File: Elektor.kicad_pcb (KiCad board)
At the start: 2 copper layers, 50 x 42 mm, 63 parts, among them J1 Conn_Coaxial, Q1 BF545B, U1 Si5351A-B-GT, U2 74HC04, U3 74HC4066D_653, U5 MCP6022, U6 AUDIOSHIELD-REVD, U7 MCP6022, Y1 ABM7-25.000MHZ-D2Y-T

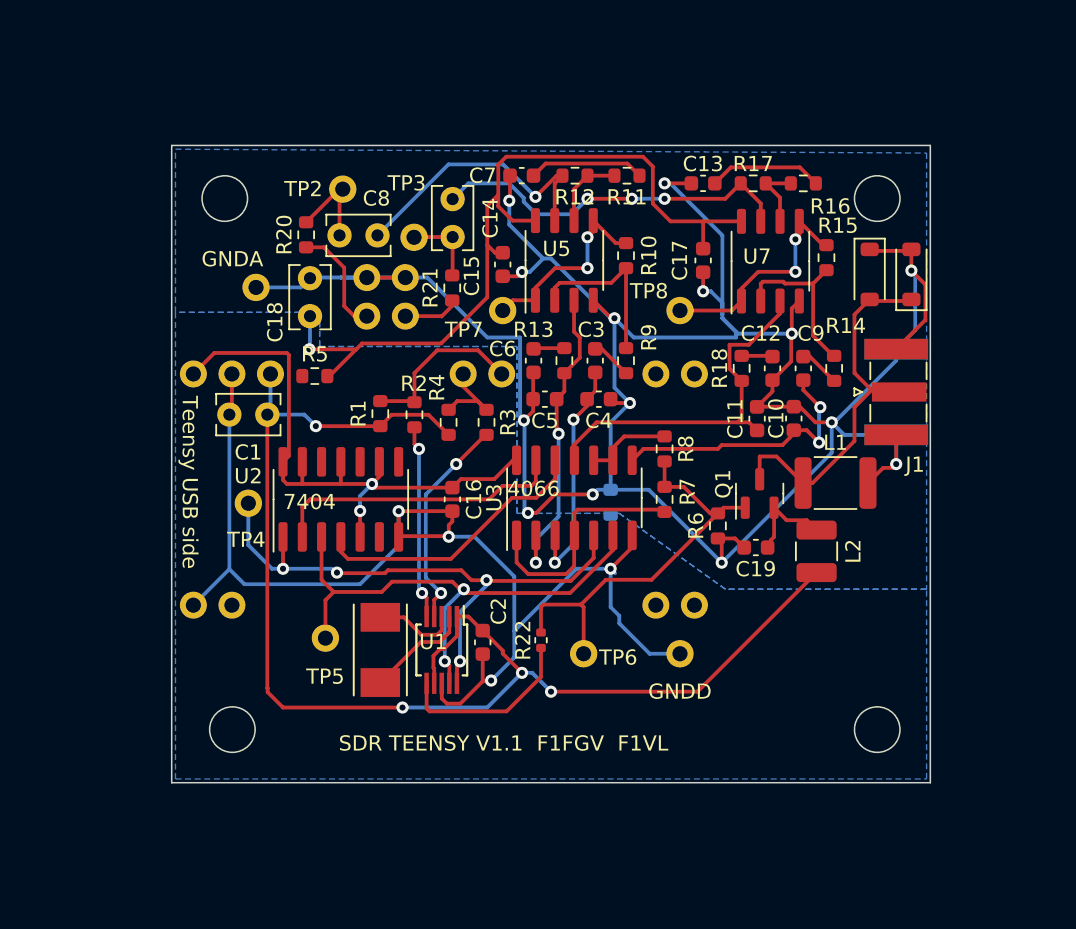
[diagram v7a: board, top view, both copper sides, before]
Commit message: version 2.0 using a SN74CBTLV3253
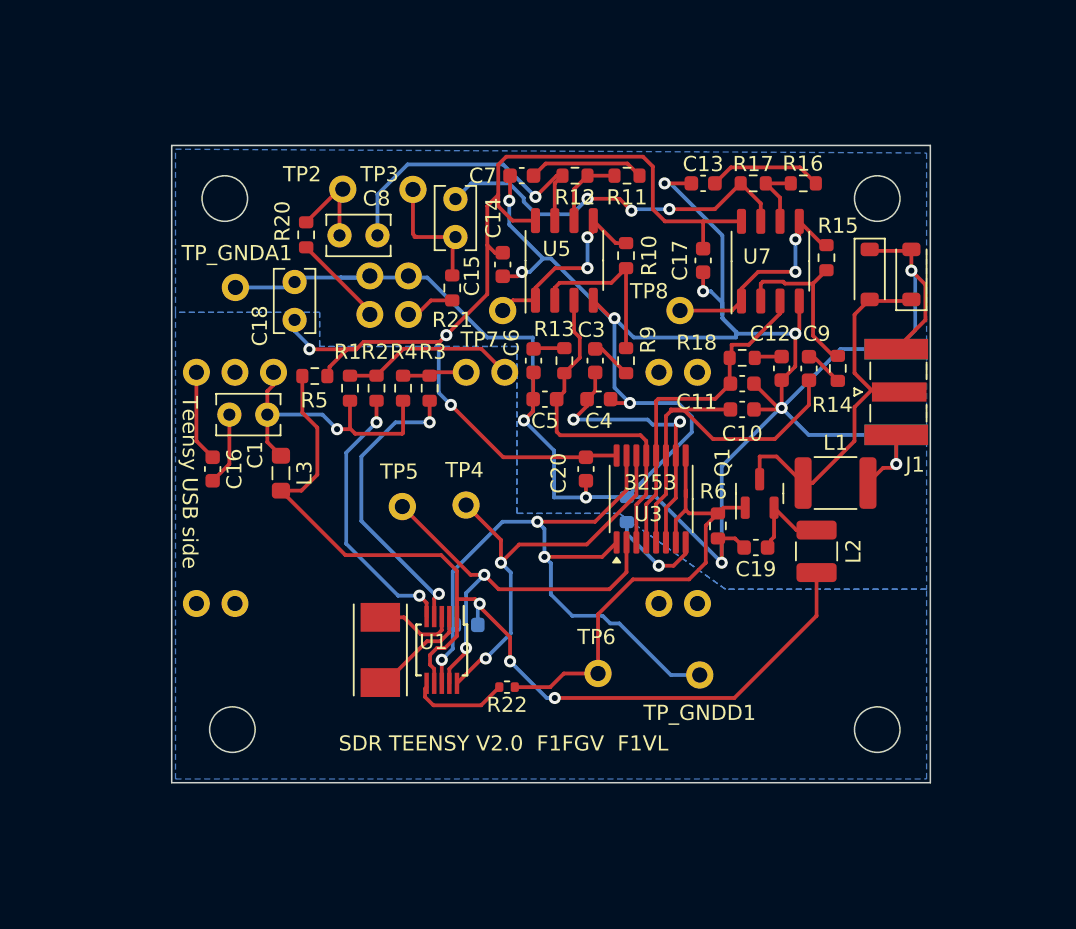
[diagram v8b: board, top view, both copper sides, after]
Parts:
- removed R7, R8: 100, Resistor_SMD:R_0603_1608Metric
- removed U2: 74HC04, Package_SO:SOIC-14_3.9x8.7mm_P1.27mm
- added C20: 100n, Capacitor_SMD:C_0603_1608Metric, F.Cu at (184.3, 82.3)
- added L3: 1uH, Inductor_SMD:L_0805_2012Metric_Pad1.05x1.20mm_HandSolder, F.Cu at (164.2, 82.6)
- C2: moved to B.Cu
- U3: value 74HC4066D_653 -> SN74CBTLV3253PW; footprint Package_SO:SOIC-14_3.9x8.7mm_P1.27mm -> Package_SO:TSSOP-16_4.4x5mm_P0.65mm
- moved C16 15.9 mm to (159.7, 82.3)
- moved TP4 14.3 mm to (176.4, 84.7)
- moved TP5 10.0 mm to (172.2, 84.8)
- moved U3 5.06 mm to (188.6, 84.3)
- moved R3 4.37 mm to (174.0, 77.0)
- moved R22 3.82 mm to (179.1, 96.7), turned to 180 degrees
- moved R2 3.75 mm to (172.2, 77.0)
- moved C10 3.45 mm to (194.6, 78.4), turned to 180 degrees
- moved TP3 3.16 mm to (172.9, 63.9)
- moved R4 3.05 mm to (170.5, 77.0)
- moved R1 2.61 mm to (168.8, 77.0)
- moved C11 2.51 mm to (194.6, 76.7), turned to 0 degrees
- moved TP_GNDD1 1.91 mm to (191.8, 95.9)
- moved TP6 1.61 mm to (185.1, 95.8)
- moved C2 1.59 mm to (176.4, 92.6), turned to 180 degrees
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- renumbered GNDA to TP_GNDA1, GNDD to TP_GNDD1
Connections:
- C1 pad 1: 3.3V -> Net-(C1-Pad1)
- C10 pad 2: Net-(U3-3Y) -> Net-(U3-1B2)
- C11 pad 1: Net-(U3-4Y) -> Net-(U3-1B3)
- C16 pad 1: Net-(U2G-VCC) -> Net-(C16-Pad1)
- C3 pad 1: Net-(U3-2Z) -> Net-(U3-1B1)
- C4 pad 2: Net-(U3-2Z) -> Net-(U3-1B1)
- C5 pad 1: Net-(U3-1Z) -> Net-(U3-1B4)
- C9 pad 1: Net-(U3-3Y) -> Net-(U3-1B2)
- R1 pad 1: 3.3V -> Net-(C1-Pad1)
- R13 pad 1: Net-(U3-1Z) -> Net-(U3-1B4)
- R18 pad 1: Net-(U3-4Y) -> Net-(U3-1B3)
- R19 pad 1: unconnected-(R19-Pad1) -> GND
- R2 pad 1: 3.3V -> Net-(C1-Pad1)
- R22 pad 1: Net-(U1-CLK2) -> Net-(Q1-S)
- R22 pad 2: Net-(Q1-S) -> Net-(U1-CLK2)
- U3 pad 1: Net-(U3-1Y) -> GND
- U3 pad 10: Net-(U3-3Z) -> Net-(U3-1B1)
- U3 pad 11: Net-(U3-4Y) -> Net-(U3-1B2)
- U3 pad 12: Net-(U3-4E) -> Net-(U3-1B3)
- U3 pad 13: Net-(U3-1E) -> Net-(U3-1B4)
- U3 pad 14: Net-(U2G-VCC) -> Net-(TP4-Pin_1)
- U3 pad 2: Net-(U3-1Z) -> Net-(TP5-Pin_1)
- U3 pad 3: Net-(U3-2Z) -> Net-(U3-1B4)
- U3 pad 4: Net-(U3-1Y) -> Net-(U3-1B3)
- U3 pad 5: Net-(TP4-Pin_1) -> Net-(U3-1B2)
- U3 pad 6: Net-(TP5-Pin_1) -> Net-(U3-1B1)
- U3 pad 7: GND -> Net-(Q1-S)
- U3 pad 8: Net-(U3-3Y) -> GND
- U3 pad 9: Net-(U3-3Z) -> Net-(Q1-S)
- U5 pad 3: Net-(U3-1Z) -> Net-(U3-1B4)
- U6 pad 3V: 3.3V -> Net-(C1-Pad1)
- U6 pad 5V: Net-(U2G-VCC) -> Net-(C16-Pad1)
- U7 pad 3: Net-(U3-4Y) -> Net-(U3-1B3)
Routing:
- net Net-(U2G-VCC): track 40.1 -> 0.00 mm, vias 2 -> 0
- net Net-(U3-1B2): track 0.00 -> 25.5 mm
- net Net-(U3-4Y): track 23.5 -> 0.00 mm
- net Net-(U3-1B4): track 0.00 -> 22.6 mm
- net GND: track 79.9 -> 57.4 mm
- net Net-(U3-1B3): track 0.00 -> 22.2 mm
- net Net-(U3-1Z): track 20.6 -> 0.00 mm, vias 2 -> 0
- net Net-(C1-Pad1): track 0.00 -> 19.5 mm, vias 0 -> 1
- net Net-(U3-1E): track 19.5 -> 0.00 mm
- net Net-(U3-1B1): track 0.00 -> 19.3 mm, vias 0 -> 2
- net 3.3V: track 86.3 -> 67.3 mm, vias 4 -> 3
- net Net-(U3-4E): track 18.7 -> 0.00 mm
- net Net-(U3-3Y): track 18.0 -> 0.00 mm, vias 2 -> 0
- net 3.3VA: track 52.9 -> 70.9 mm, vias 1 -> 3
- net Net-(U3-1Y): track 15.5 -> 0.00 mm
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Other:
- board text added: "3253"
- board text added: "SDR TEENSY V2.0 F1FGV F1VL"
- board text removed: "4066"
- board text removed: "7404"
- board text removed: "SDR TEENSY V1.1 F1FGV F1VL"
